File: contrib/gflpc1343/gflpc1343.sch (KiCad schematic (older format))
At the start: 38 parts, among them J1 USB-MICRO-B, P1 GOODFET, P2 SWD, P3 ISP, P4 EXPANSION, Q1 PNP, U1 LPC1343FBD48, U2 AP7333, X1 XTAL4PIN

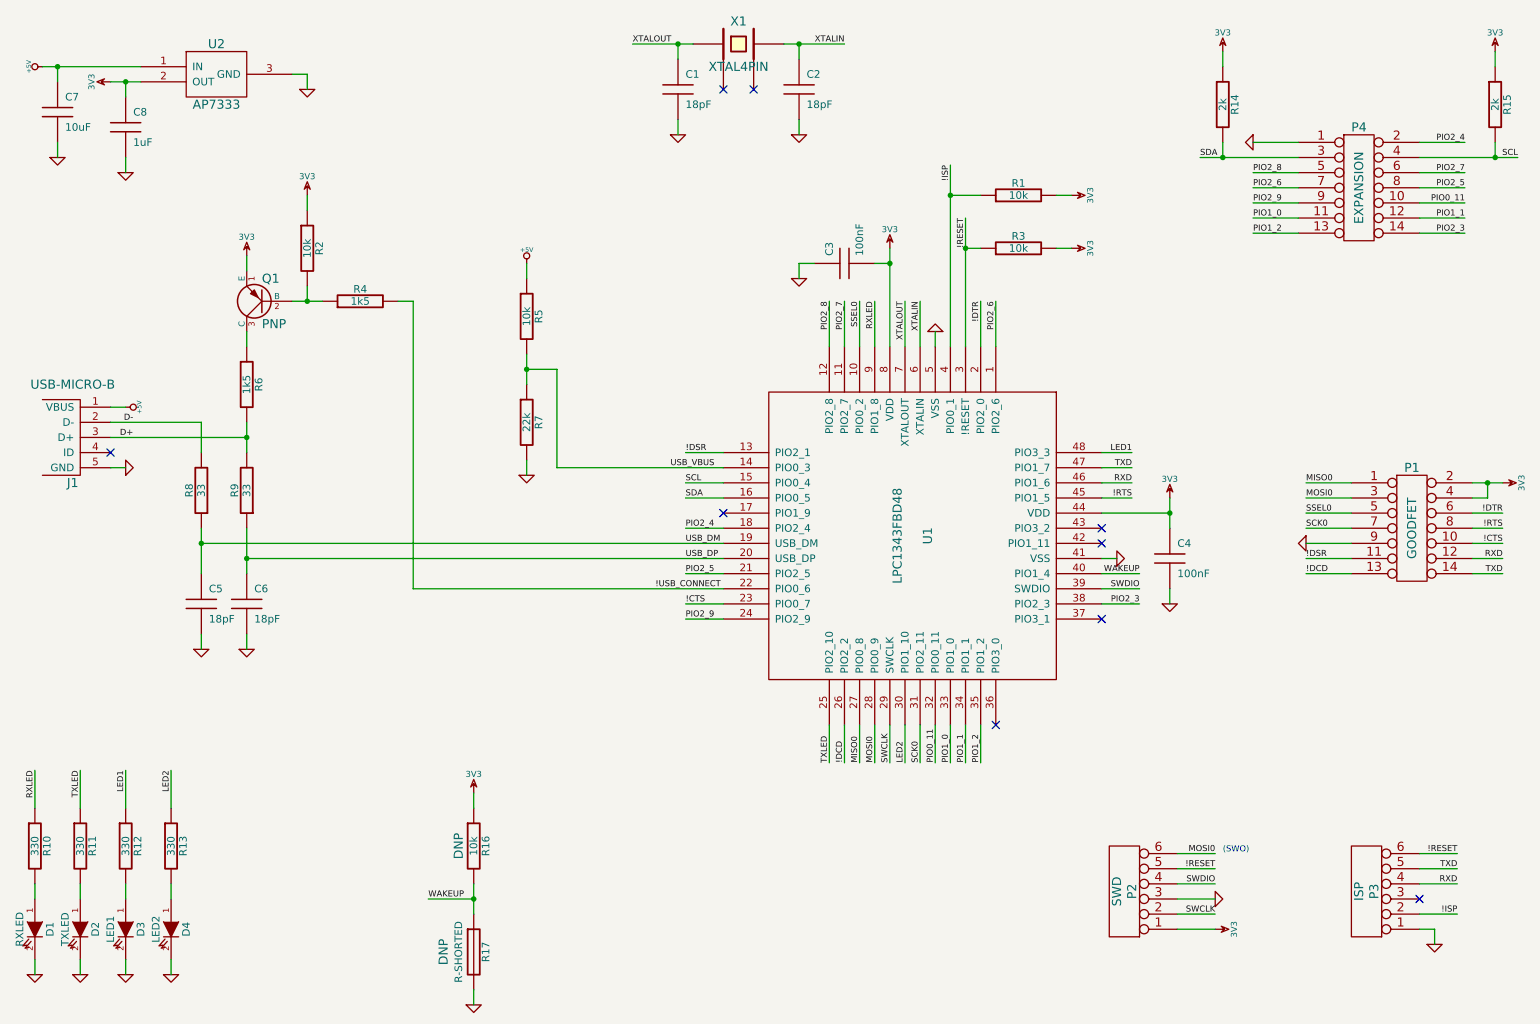
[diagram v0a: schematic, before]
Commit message: gflpc1343: brought 3V3 and 5V to expansion header
git-svn-id: https://svn.code.sf.net/p/goodfet/code@1255 12e2690d-a6be-4b82-a7b7-67c4a43b65c8
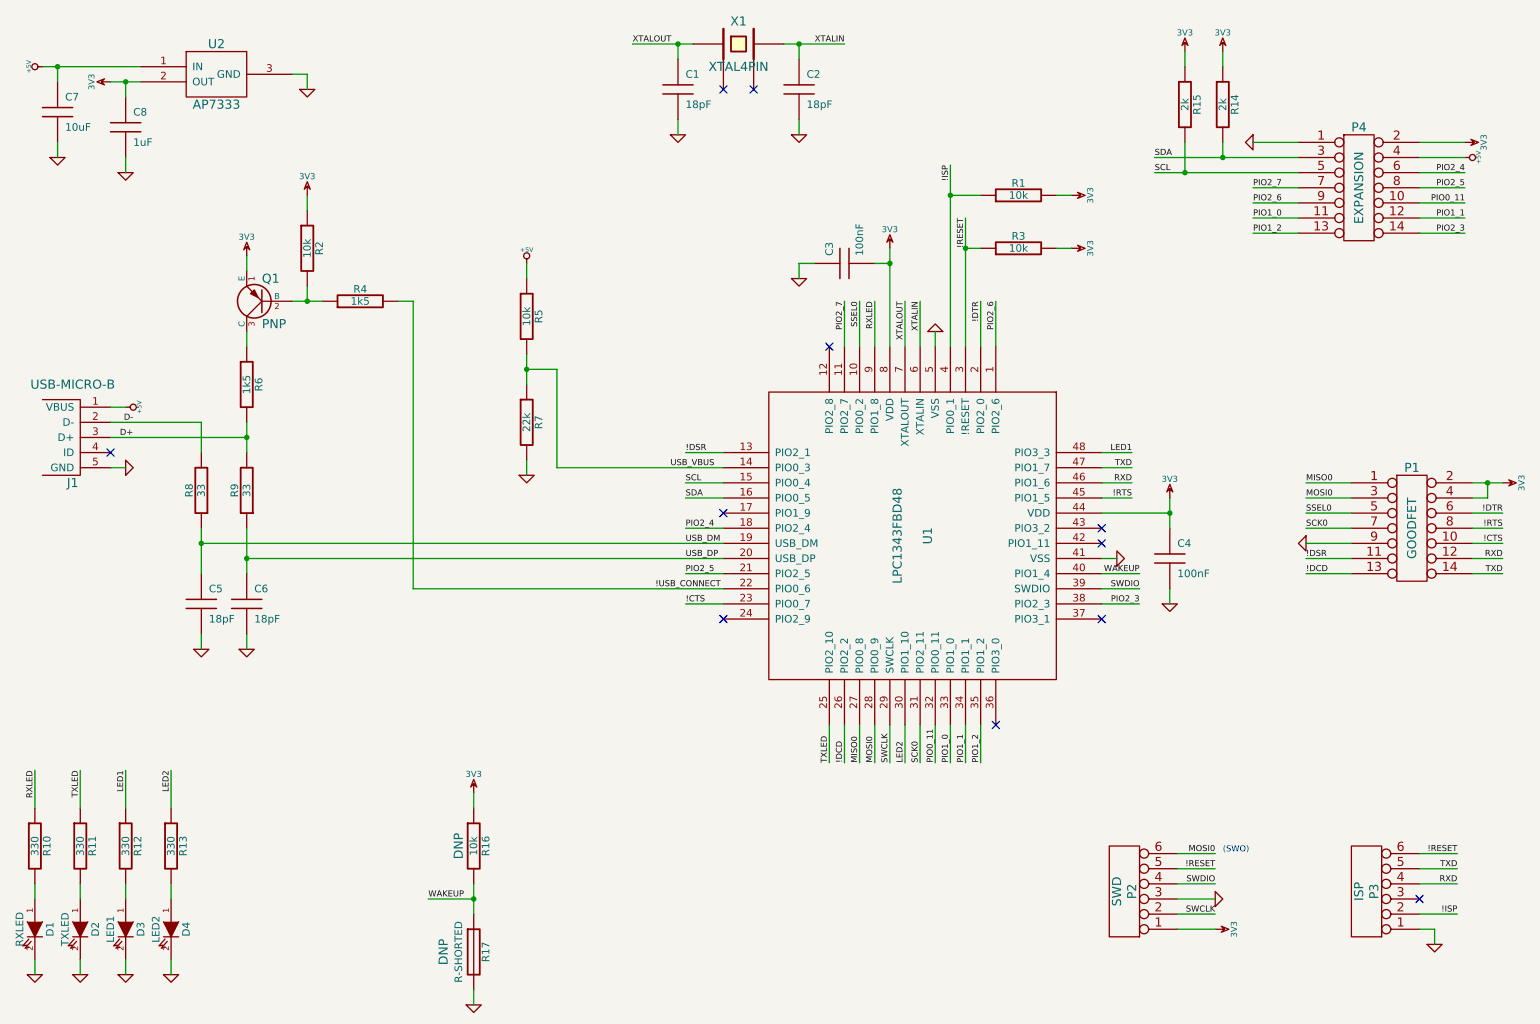
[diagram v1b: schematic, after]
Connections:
- net +5V: now also P4.4 (P4)
- net 3V3: now also P4.2 (P2)
- net PIO2_4: now also P4.6 (P6); no longer P4.2 (P2)
- net PIO2_6: now also P4.9; no longer P4.7 (P7)
- net PIO2_7: now also P4.7 (P7); no longer P4.6 (P6)
- net SCL: now also P4.5 (P5); no longer P4.4 (P4)
- net PIO2_8: no longer names the net of U1.12 (PIO2_8)
- net PIO2_8: no longer P4.5 (P5)
- net PIO2_9: no longer names the net of U1.24 (PIO2_9)
- net PIO2_9: no longer P4.9
- no-connect marks 9 -> 11
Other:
- moved on the sheet: R15
